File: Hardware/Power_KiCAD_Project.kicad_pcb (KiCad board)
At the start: 4 copper layers, 80 x 93.8 mm, 74 parts, among them IC1 STM32L562VET6Q, J1 XT60-M, J2 XT60-M, J3 XT60-M, J4 XT60-M, J5 XT60-M, J6 PJ-102AH, J7 XT60-M, J8 L717SDC37P1ACH4F, Q1 BSS84PH6327XTSA2, SW1 Reboot, U1 MCP9808_MSOP, U2 MCP9808_MSOP, U3 LM2678SX-5.0/NOPB, U4 LM2678SX-3.3/NOPB, U5 BQ76920PW, U6 PSMN2R6-40YS, U7 PSMN2R6-40YS, Y1 Crystal

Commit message: Added 3d step models to every component
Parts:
- removed IC1: STM32L562VET6Q, SamacSys_Parts:QFP50P1600X1600X160-100N
- removed U7: PSMN2R6-40YS, TO127P600X120-5N:TO127P600X120-5N
- removed VR1: T93YA103KT20, SamacSys_Parts:T93YA5K10
- added C30: 100nF, Capacitor_SMD:C_0603_1608Metric_Pad1.08x0.95mm_HandSolder, F.Cu at (328.5, 107.2)
- added C31: 100nF, Capacitor_SMD:C_0603_1608Metric_Pad1.08x0.95mm_HandSolder, F.Cu at (319.8, 115.0)
- added C32: 100nF, Capacitor_SMD:C_0603_1608Metric_Pad1.08x0.95mm_HandSolder, F.Cu at (319.8, 117.6)
- added C33: 100nF, Capacitor_SMD:C_0603_1608Metric_Pad1.08x0.95mm_HandSolder, F.Cu at (319.8, 107.5)
- added C34: 100nF, Capacitor_SMD:C_0603_1608Metric_Pad1.08x0.95mm_HandSolder, F.Cu at (328.5, 109.7)
- added C35: 100nF, Capacitor_SMD:C_0603_1608Metric_Pad1.08x0.95mm_HandSolder, F.Cu at (324.2, 115.0)
- added C36: 100nF, Capacitor_SMD:C_0603_1608Metric_Pad1.08x0.95mm_HandSolder, F.Cu at (182.9, 95.5)
- added Q2: BSS84PH6327XTSA2, Package_TO_SOT_SMD:SOT-23, F.Cu at (272.3, 130.0)
- added Q3: PSMN2R6-40YS, Package_TO_SOT_SMD:LFPAK33, F.Cu at (272.8, 125.3)
- added R18: 4.7k, Resistor_SMD:R_0603_1608Metric_Pad1.05x0.95mm_HandSolder, F.Cu at (324.2, 117.6)
- added R19: 4.7k, Resistor_SMD:R_0603_1608Metric_Pad1.05x0.95mm_HandSolder, F.Cu at (319.8, 120.1)
- added RV1: 10Ω to 2.2MΩ, RDT_Custom_Footprints:T93YA5K10, F.Cu at (256.4, 131.1)
- C1, C22: footprint Capacitor_SMD:C_0603_1608Metric -> Capacitor_SMD:C_0603_1608Metric_Pad1.08x0.95mm_HandSolder
- C10: value 35SVPF82M -> 16SVP330M; footprint SamacSys_Parts:16SVPT560M -> RDT_Custom_Footprints:16SVF1000M; moved to F.Cu
- C11, C12: value C0805C104M5RACTU -> 1μF; footprint SamacSys_Parts:CAPC2012X88N -> Capacitor_SMD:C_0603_1608Metric_Pad1.08x0.95mm_HandSolder; moved to F.Cu
- C13, C14: value CGA4C2C0G1H103J060AA -> 1μF; footprint SamacSys_Parts:CAPC2012X75N -> Capacitor_SMD:C_0603_1608Metric_Pad1.08x0.95mm_HandSolder; moved to F.Cu
- C15: value 16SVP330M -> 1μF; footprint SamacSys_Parts:16SVF1000M -> Capacitor_SMD:C_0603_1608Metric_Pad1.08x0.95mm_HandSolder; moved to F.Cu
- C16: value 6SVPC330M -> 1μF; footprint SamacSys_Parts:16SVF180M -> Capacitor_SMD:C_0603_1608Metric_Pad1.08x0.95mm_HandSolder; moved to F.Cu
- C17: value 1μF -> 4.7μF; footprint Capacitor_SMD:C_0603_1608Metric -> Capacitor_SMD:C_0603_1608Metric_Pad1.08x0.95mm_HandSolder
- C18, C20, C21: value 1μF -> 0.1μF; footprint Capacitor_SMD:C_0603_1608Metric -> Capacitor_SMD:C_0603_1608Metric_Pad1.08x0.95mm_HandSolder
- C19: value 1μF -> 10μF; footprint Capacitor_SMD:C_0603_1608Metric -> Capacitor_SMD:C_0603_1608Metric_Pad1.08x0.95mm_HandSolder
- C2: value 1uF -> 100nF; footprint Capacitor_SMD:C_0603_1608Metric -> Capacitor_SMD:C_0603_1608Metric_Pad1.08x0.95mm_HandSolder
- C23: value 0.1μF -> 1μF; footprint Capacitor_SMD:C_0603_1608Metric -> Capacitor_SMD:C_0603_1608Metric_Pad1.08x0.95mm_HandSolder
- C24: value 0.1μF -> 30pF; footprint Capacitor_SMD:C_0603_1608Metric -> Capacitor_SMD:C_0603_1608Metric_Pad1.08x0.95mm_HandSolder
- C25: value 4.7μF -> 30pF; footprint Capacitor_SMD:C_0603_1608Metric -> Capacitor_SMD:C_0603_1608Metric_Pad1.08x0.95mm_HandSolder
- C26: value 0.1μF -> 1uF; footprint Capacitor_SMD:C_0603_1608Metric -> Capacitor_SMD:C_0603_1608Metric_Pad1.08x0.95mm_HandSolder
- C27, C28: value 1μF -> 100nF; footprint Capacitor_SMD:C_0603_1608Metric -> Capacitor_SMD:C_0603_1608Metric_Pad1.08x0.95mm_HandSolder
- C29: value 10μF -> 100nF; footprint Capacitor_SMD:C_0603_1608Metric -> Capacitor_SMD:C_0603_1608Metric_Pad1.08x0.95mm_HandSolder
- C3, C4: value 100nF -> 35SVPF82M; footprint Capacitor_SMD:C_0603_1608Metric -> RDT_Custom_Footprints:16SVPT560M
- C5, C6: value 30pF -> C0805C104M5RACTU; footprint Capacitor_SMD:C_0603_1608Metric -> RDT_Custom_Footprints:CAPC2012X88N
- C7, C8: value 100nF -> CGA4C2C0G1H103J060AA; footprint Capacitor_SMD:C_0603_1608Metric -> RDT_Custom_Footprints:CAPC2012X75N
- C9: value 35SVPF82M -> 6SVPC330M; footprint SamacSys_Parts:16SVPT560M -> RDT_Custom_Footprints:16SVF180M; moved to F.Cu
- D1: value GREEN -> SBRD10200TR; footprint LED_SMD:LED_0603_1608Metric -> Package_TO_SOT_SMD:TO-252-2
- D2: value RED -> SBRD10200TR; footprint LED_SMD:LED_0603_1608Metric -> Package_TO_SOT_SMD:TO-252-2
- D3: value SBRD10200TR -> LED; footprint SBRD10200TR:DPAK228P1005X240-4N -> LED_SMD:LED_0603_1608Metric; moved to F.Cu
- D4: value SBRD10200TR -> 1N4148W-7-F; footprint SBRD10200TR:DPAK228P1005X240-4N -> Diode_SMD:D_SOD-123; moved to F.Cu
- D5: value LED -> GREEN
- D6: value 1N4148W-7-F -> RED; footprint SamacSys_Parts:SOD3716X145N -> LED_SMD:LED_0603_1608Metric
- J1: value XT60-M -> Barrel_Jack_MountingPin; footprint XT60-M:AMASS_XT60-M -> Connector_BarrelJack:BarrelJack_CUI_PJ-102AH_Horizontal; moved to F.Cu
- J2: value XT60-M -> XT60 Cell 5; footprint XT60-M:AMASS_XT60-M -> RDT_Custom_Footprints:AMASS_XT60-M; moved to F.Cu
- J3: value XT60-M -> XT60 Cell 4; footprint XT60-M:AMASS_XT60-M -> RDT_Custom_Footprints:AMASS_XT60-M; moved to F.Cu
- J4: value XT60-M -> XT60 Cell 3; footprint XT60-M:AMASS_XT60-M -> RDT_Custom_Footprints:AMASS_XT60-M; moved to F.Cu
- J5: value XT60-M -> XT60 Cell 2; footprint XT60-M:AMASS_XT60-M -> RDT_Custom_Footprints:AMASS_XT60-M; moved to F.Cu
- J6: value PJ-102AH -> XT60 Cell 1; footprint SamacSys_Parts:PJ-102AH -> RDT_Custom_Footprints:AMASS_XT60-M; moved to F.Cu
- J7: value XT60-M -> XT60 To External Switch; footprint XT60-M:AMASS_XT60-M -> RDT_Custom_Footprints:AMASS_XT60-M
- J8: footprint SamacSys_Parts:L717SDC37P1ACH4F -> RDT_Custom_Footprints:L717SDC37P1ACH4F; moved to F.Cu
- L1: value SRP1270-8R2M -> MSS1210-153MEB; footprint SamacSys_Parts:INDPM137129X700N -> RDT_Custom_Footprints:IND_MSS1210-153MEB; moved to F.Cu
- L2: value MSS1210-153MEB -> SRP1270-8R2M; footprint MSS1210-153MEB:IND_MSS1210-153MEB -> RDT_Custom_Footprints:INDPM137129X700N; moved to F.Cu
- Q1: value BSS84PH6327XTSA2 -> PSMN2R6-40YS; footprint SamacSys_Parts:SOT95P240X110-3N -> Package_TO_SOT_SMD:LFPAK33
- R1, R11, R2: value 1k5Ω -> 100Ω; footprint Resistor_SMD:R_0603_1608Metric -> Resistor_SMD:R_0603_1608Metric_Pad1.05x0.95mm_HandSolder
- R10: value WSHP28185L000FEA -> 5mΩ 10W
- R12: value 10kΩ -> 1MΩ; footprint Resistor_SMD:R_0603_1608Metric -> Resistor_SMD:R_0603_1608Metric_Pad1.05x0.95mm_HandSolder
- R13, R15: value 100Ω -> 1MΩ; footprint Resistor_SMD:R_0603_1608Metric -> Resistor_SMD:R_0603_1608Metric_Pad1.05x0.95mm_HandSolder
- R14: value 1MΩ -> 10kΩ; footprint Resistor_SMD:R_0603_1608Metric -> Resistor_SMD:R_0603_1608Metric_Pad1.05x0.95mm_HandSolder
- R16, R17: value 1MΩ -> 1k5Ω; footprint Resistor_SMD:R_0603_1608Metric -> Resistor_SMD:R_0603_1608Metric_Pad1.05x0.95mm_HandSolder
- R3, R4, R5, R6, R8, R9: footprint Resistor_SMD:R_0603_1608Metric -> Resistor_SMD:R_0603_1608Metric_Pad1.05x0.95mm_HandSolder
- R7: value 100Ω -> 1k5Ω; footprint Resistor_SMD:R_0603_1608Metric -> Resistor_SMD:R_0603_1608Metric_Pad1.05x0.95mm_HandSolder
- SW1: footprint Button_Switch_SMD:SW_Push_1P1T_NO_6x6mm_H9.5mm -> Button_Switch_SMD:SW_SPST_PTS645
- U3, U4: moved to F.Cu
- U6: value PSMN2R6-40YS -> STM32L562VET; footprint TO127P600X120-5N:TO127P600X120-5N -> Package_QFP:LQFP-100_14x14mm_P0.5mm
- Y1: value Crystal -> 32MHz; footprint Crystal:Crystal_HC49-4H_Vertical -> Crystal:Crystal_SMD_2012-2Pin_2.0x1.2mm_HandSoldering
- moved R17 210.7 mm to (328.5, 112.2), turned to 0 degrees
- moved D6 207.5 mm to (324.0, 120.1), turned to 0 degrees
- moved C29 205.2 mm to (324.2, 110.0), turned to 0 degrees
- moved D5 205.2 mm to (328.4, 114.7), turned to 0 degrees
- moved C27 203.7 mm to (328.6, 104.7), turned to 0 degrees
- moved R16 202.9 mm to (324.2, 112.5), turned to 0 degrees
- moved C24 200.0 mm to (324.3, 104.7), turned to 0 degrees
- moved C28 199.1 mm to (319.8, 112.5), turned to 0 degrees
- moved C26 196.4 mm to (324.2, 107.5)
- moved C25 193.9 mm to (319.8, 110.0), turned to 0 degrees
- moved Y1 187.1 mm to (319.9, 104.8), turned to 0 degrees
- moved U6 180.2 mm to (308.4, 112.7), turned to 0 degrees
- moved R15 173.6 mm to (284.4, 132.2), turned to 0 degrees
- moved R11 168.3 mm to (292.1, 118.8)
- moved C23 165.6 mm to (287.7, 122.2), turned to 0 degrees
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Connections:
- C1 pad 2: /Pack- -> GND
- C10 pad 1: /PACK_M5 -> +5V
- C10 pad 2: /Pack- -> GND
- C11 pad 1: /PACK_M5 -> /LiPo Pack Monitor/VC5
- C11 pad 2: /Pack- -> /LiPo Pack Monitor/VC4
- C12 pad 1: /PACK_M5 -> /LiPo Pack Monitor/VC4
- C12 pad 2: /Pack- -> /LiPo Pack Monitor/VC3
- C13 pad 1: Net-(C13-Pad1) -> /LiPo Pack Monitor/VC3
- C13 pad 2: Net-(C13-Pad2) -> /LiPo Pack Monitor/VC2
- C14 pad 1: Net-(C14-Pad1) -> /LiPo Pack Monitor/VC2
- C14 pad 2: Net-(C14-Pad2) -> /LiPo Pack Monitor/VC1
- C15 pad 1: +5V -> /LiPo Pack Monitor/VC1
- C15 pad 2: /Pack- -> GNDREF
- C16 pad 1: +3V3 -> GNDREF
- C16 pad 2: /Pack- -> /LiPo Pack Monitor/VC0
- C17 pad 1: /LiPo Pack Monitor/VC5 -> GNDREF
- C17 pad 2: /LiPo Pack Monitor/VC4 -> Net-(C17-Pad2)
- C18 pad 1: /LiPo Pack Monitor/VC4 -> Net-(C18-Pad1)
- C18 pad 2: /LiPo Pack Monitor/VC3 -> GNDREF
- C19 pad 1: /LiPo Pack Monitor/VC3 -> GNDREF
- C19 pad 2: /LiPo Pack Monitor/VC2 -> Net-(C19-Pad2)
- C2 pad 1: /Pack- -> +3V3
- C2 pad 2: +3V3 -> GND
- C20 pad 1: /LiPo Pack Monitor/VC2 -> Net-(C20-Pad1)
- C20 pad 2: /LiPo Pack Monitor/VC1 -> Net-(C18-Pad1)
- C21 pad 1: /LiPo Pack Monitor/VC1 -> GNDREF
- C21 pad 2: GND -> Net-(C20-Pad1)
- C22 pad 1: GND -> GNDREF
- C22 pad 2: /LiPo Pack Monitor/VC0 -> /PACK_M5
- C23 pad 1: /LiPo Pack Monitor/SRP -> GNDREF
- C23 pad 2: GND -> Net-(C23-Pad2)
- C24 pad 1: /LiPo Pack Monitor/SRN -> Net-(C24-Pad1)
- C24 pad 2: /LiPo Pack Monitor/SRP -> GND
- C25 pad 1: GND -> Net-(C25-Pad1)
- C25 pad 2: Net-(C25-Pad2) -> GND
- C26 pad 1: GND -> +3V3
- C26 pad 2: /LiPo Pack Monitor/SRN -> GND
- C27 pad 1: GND -> +3V3
- C27 pad 2: Net-(C27-Pad2) -> GND
- C28 pad 1: GND -> +3V3
- C28 pad 2: /PACK_M5 -> GND
- C29 pad 1: GND -> +3V3
- C29 pad 2: /LiPo Pack Monitor/BAT -> GND
- C3 pad 1: /Pack- -> /PACK_M5
- C3 pad 2: +3V3 -> GND
- C4 pad 1: /Pack- -> /PACK_M5
- C4 pad 2: +3V3 -> GND
- C5 pad 1: /Pack- -> /PACK_M5
- C5 pad 2: Net-(C5-Pad2) -> GND
- C6 pad 1: /Pack- -> /PACK_M5
- C6 pad 2: Net-(C6-Pad2) -> GND
- C7 pad 1: +3V3 -> Net-(C7-Pad1)
- C7 pad 2: /Pack- -> Net-(C7-Pad2)
- C8 pad 1: /NRST -> Net-(C8-Pad1)
- C8 pad 2: /Pack- -> Net-(C8-Pad2)
- C9 pad 1: /PACK_M5 -> +3V3
- C9 pad 2: /Pack- -> GND
- D1 pad 1: Net-(D1-Pad1) -> GND
- D1 pad 2: Net-(D1-Pad2) -> Net-(C7-Pad2)
- D2 pad 1: Net-(D2-Pad1) -> GND
- D2 pad 2: Net-(D2-Pad2) -> Net-(C8-Pad2)
- D3 pad 1: /Pack- -> Net-(D3-Pad1)
- D3 pad 2: Net-(C13-Pad2) -> Net-(C17-Pad2)
- D4 pad 1: /Pack- -> Net-(D4-Pad1)
- D4 pad 2: Net-(C14-Pad2) -> Net-(D4-Pad2)
- D5 pad 2: Net-(C25-Pad2) -> Net-(D5-Pad2)
- J1 pad 1: /PACK_M4 -> /PACK_M5
- J1 pad 2: /PACK_M5 -> GNDREF
- J2 pad 1: /PACK_M3 -> /PACK_M4
- J2 pad 2: /PACK_M4 -> /PACK_M5
- J3 pad 1: /PACK_M2 -> /PACK_M3
- J3 pad 2: /PACK_M3 -> /PACK_M4
- J4 pad 1: /PACK_M1 -> /PACK_M2
- J4 pad 2: /PACK_M2 -> /PACK_M3
- J5 pad 1: GND -> /PACK_M1
- J5 pad 2: /PACK_M1 -> /PACK_M2
- J6 pad 1: /PACK_M5 -> GNDREF
- J6 pad 2: /Pack- -> /PACK_M1
- J7 pad 1: GND -> GNDREF
- J7 pad 2: GND -> Net-(J7-Pad2)
- J8 pad 1: /Pack- -> GND
- J8 pad 10: (no net) -> Net-(J8-Pad10)
- J8 pad 11: (no net) -> Net-(J8-Pad11)
- J8 pad 12: (no net) -> Net-(J8-Pad12)
- J8 pad 13: (no net) -> Net-(J8-Pad13)
- J8 pad 14: (no net) -> Net-(J8-Pad14)
- J8 pad 15: (no net) -> Net-(J8-Pad15)
- J8 pad 16: (no net) -> Net-(J8-Pad16)
- J8 pad 17: (no net) -> Net-(J8-Pad17)
- J8 pad 19: /Pack- -> GND
- J8 pad 21: (no net) -> /DSUB-37_Bus/t_mosi
- J8 pad 22: (no net) -> /DSUB-37_Bus/t_clk
- J8 pad 23: /SWCLK -> /STM32L562VET6Q 1/DEBUG_SWCLK
- J8 pad 24: /Alert_sda -> /DSUB-37_Bus/Alert_sda
- J8 pad 25: /NRST -> /DSUB-37_Bus/NRST
- J8 pad 26: (no net) -> /DSUB-37_Bus/Fire_redundant
- J8 pad 27: (no net) -> Net-(J8-Pad27)
- J8 pad 28: (no net) -> Net-(J8-Pad28)
- J8 pad 29: (no net) -> Net-(J8-Pad29)
- J8 pad 3: (no net) -> /DSUB-37_Bus/t_miso
- J8 pad 30: (no net) -> Net-(J8-Pad30)
- J8 pad 31: (no net) -> Net-(J8-Pad31)
- J8 pad 32: (no net) -> Net-(J8-Pad32)
- J8 pad 33: (no net) -> Net-(J8-Pad33)
- J8 pad 34: (no net) -> Net-(J8-Pad34)
- J8 pad 35: (no net) -> Net-(J8-Pad35)
- J8 pad 36: (no net) -> Net-(J8-Pad36)
- J8 pad 4: /SWDIO -> /STM32L562VET6Q 1/DEBUG_SWDIO
- J8 pad 5: /Alert_scl -> /DSUB-37_Bus/Alert_scl
- J8 pad 6: /Alert_active -> /DSUB-37_Bus/Alert_Active
- J8 pad 7: (no net) -> /DSUB-37_Bus/Fire
- J8 pad 8: (no net) -> Net-(J8-Pad8)
- J8 pad 9: (no net) -> Net-(J8-Pad9)
- J8 pad MH1: /Pack- -> GND
- J8 pad MH2: /Pack- -> GND
- L1 pad 1: Net-(C14-Pad2) -> Net-(C7-Pad2)
- L1 pad 2: +3V3 -> +5V
- L2 pad 1: Net-(C13-Pad2) -> Net-(C8-Pad2)
- L2 pad 2: +5V -> +3V3
- Q1 pad 1: GND -> Net-(Q1-Pad1)
- Q1 pad 2: Net-(D6-Pad2) -> Net-(Q1-Pad1)
- Q1 pad 3: Net-(Q1-Pad3) -> Net-(Q1-Pad1)
- R1 pad 1: Net-(D1-Pad1) -> /PACK_M5
- R1 pad 2: /Pack- -> /LiPo Pack Monitor/VC5
- R10 pad 1: GND -> Net-(J7-Pad2)
- R10 pad 2: Net-(R10-Pad2) -> Net-(Q1-Pad1)
- R11 pad 1: Net-(D5-Pad1) -> Net-(C20-Pad1)
- R11 pad 2: GND -> Net-(Q1-Pad1)
- R12 pad 1: /LiPo Pack Monitor/TS1 -> Net-(Q1-Pad4)
- R12 pad 2: Net-(R12-Pad2) -> Net-(Q1-Pad1)
- R13 pad 1: /LiPo Pack Monitor/SRN -> Net-(D4-Pad1)
- R13 pad 2: Net-(R10-Pad2) -> Net-(D4-Pad2)
- R14 pad 2: Net-(R10-Pad2) -> Net-(R14-Pad2)
- R15 pad 1: /PACK_M5 -> Net-(D4-Pad1)
- R15 pad 2: /LiPo Pack Monitor/BAT -> GNDREF
- R16 pad 1: Net-(D6-Pad1) -> Net-(D5-Pad1)
- R16 pad 2: Net-(D6-Pad2) -> GND
- R17 pad 2: /Pack- -> GND
- R2 pad 1: Net-(D2-Pad1) -> /PACK_M4
- R2 pad 2: /Pack- -> /LiPo Pack Monitor/VC4
- R3 pad 1: /PACK_M5 -> /PACK_M3
- R3 pad 2: /LiPo Pack Monitor/VC5 -> /LiPo Pack Monitor/VC3
- R4 pad 1: /PACK_M4 -> /PACK_M2
- R4 pad 2: /LiPo Pack Monitor/VC4 -> /LiPo Pack Monitor/VC2
- R5 pad 1: /PACK_M3 -> /PACK_M1
- R5 pad 2: /LiPo Pack Monitor/VC3 -> /LiPo Pack Monitor/VC1
- R6 pad 1: /PACK_M2 -> GNDREF
- R6 pad 2: /LiPo Pack Monitor/VC2 -> /LiPo Pack Monitor/VC0
- R7 pad 1: /PACK_M1 -> Net-(D3-Pad1)
- R7 pad 2: /LiPo Pack Monitor/VC1 -> GNDREF
- R8 pad 1: GND -> Net-(C18-Pad1)
- R8 pad 2: /LiPo Pack Monitor/VC0 -> Net-(J7-Pad2)
- R9 pad 1: /LiPo Pack Monitor/SRP -> /PACK_M5
- R9 pad 2: GND -> Net-(C19-Pad2)
- SW1 pad 1: Net-(R12-Pad2) -> Net-(R14-Pad2)
- U1 pad 4: /Pack- -> GND
- U1 pad 5: /Pack- -> GND
- U1 pad 6: /Pack- -> GND
- U1 pad 7: /Pack- -> GND
- U2 pad 4: /Pack- -> GND
- U2 pad 5: /Pack- -> GND
- U2 pad 6: /Pack- -> GND
- U3 pad 1: Net-(C13-Pad2) -> Net-(C7-Pad2)
- U3 pad 3: Net-(C13-Pad1) -> Net-(C7-Pad1)
- U3 pad 4: /Pack- -> GND
- U3 pad 7: (no net) -> Net-(U3-Pad7)
- U4 pad 1: Net-(C14-Pad2) -> Net-(C8-Pad2)
- U4 pad 3: Net-(C14-Pad1) -> Net-(C8-Pad1)
- U4 pad 4: /Pack- -> GND
- U4 pad 7: (no net) -> Net-(U4-Pad7)
- U5 pad 1: Net-(R14-Pad1) -> Net-(Q1-Pad4)
- U5 pad 10: /LiPo Pack Monitor/BAT -> Net-(C19-Pad2)
- U5 pad 11: (no net) -> Net-(U5-Pad11)
- U5 pad 18: /LiPo Pack Monitor/SRP -> Net-(C18-Pad1)
- U5 pad 19: /LiPo Pack Monitor/SRN -> Net-(C20-Pad1)
- U5 pad 2: Net-(Q1-Pad3) -> Net-(Q2-Pad3)
- U5 pad 20: (no net) -> /BATT_ALERT
- U5 pad 3: GND -> GNDREF
- U5 pad 4: (no net) -> /LiPo Pack Monitor/I2C_SDA
- U5 pad 5: (no net) -> /LiPo Pack Monitor/I2C_SCL
- U5 pad 6: /LiPo Pack Monitor/TS1 -> Net-(R14-Pad1)
- U5 pad 7: Net-(C27-Pad2) -> Net-(C23-Pad2)
- U5 pad 8: Net-(C25-Pad2) -> Net-(C17-Pad2)
- U6 pad 1: Net-(R10-Pad2) -> Net-(U6-Pad1)
- U6 pad 2: Net-(R10-Pad2) -> Net-(U6-Pad2)
- U6 pad 3: Net-(R10-Pad2) -> Net-(U6-Pad3)
- U6 pad 4: Net-(R14-Pad1) -> Net-(U6-Pad4)
- Y1 pad 1: Net-(C5-Pad2) -> Net-(C24-Pad1)
- Y1 pad 2: Net-(C6-Pad2) -> Net-(C25-Pad1)
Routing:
- net /Pack-: track 301.0 -> 0.00 mm
- net +3V3: track 281.2 -> 0.00 mm, vias 1 -> 0
- net /PACK_M5: track 209.9 -> 0.00 mm
- net +5V: track 135.7 -> 0.00 mm
- net GND: track 125.7 -> 0.00 mm, vias 2 -> 0
- net /I2C_SDA: track 74.6 -> 0.00 mm, vias 2 -> 0
- net /I2C_SCL: track 73.3 -> 0.00 mm, vias 2 -> 0
- net /TEMP_ALERT_1: track 69.9 -> 0.00 mm, vias 2 -> 0
- net /LiPo Pack Monitor/VC1: track 67.7 -> 0.00 mm, vias 2 -> 0
- net Net-(C13-Pad2): track 67.0 -> 0.00 mm
- net /SWCLK: track 62.3 -> 0.00 mm, vias 1 -> 0
- net Net-(C14-Pad2): track 58.7 -> 0.00 mm
- net /SWDIO: track 57.8 -> 0.00 mm, vias 1 -> 0
- net /LiPo Pack Monitor/VC3: track 57.2 -> 0.00 mm, vias 2 -> 0
- net /TEMP_ALERT_2: track 56.3 -> 0.00 mm, vias 2 -> 0
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- added copper zone on 3.3V.Cu, net +3V3
- added copper zone on GND.Cu, net GND
- removed copper zone on ground, net /Pack-
- removed copper zone on ground, net GND
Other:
- board size 80 x 93.8 mm -> 80 x 93.2 mm
- net class DIFF_90_USB added: clearance 0.05, trace_width 0.175006, via_dia 0.4, via_drill 0.2
- net class Default: clearance 0.2 -> 0.05
- rule pad_to_mask_clearance: 0 -> 0.051
- rule trace_clearance: 0.2 -> 0.05
- rule trace_min: 0.2 -> 0.09
- rule via_min_drill: 0.3 -> 0.2

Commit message: Progress made to the battery section
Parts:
- moved R11 184.2 mm to (108.0, 113.0)
- moved R8 181.6 mm to (108.0, 114.8)
- moved C21 179.3 mm to (104.2, 113.0)
- moved R12 173.0 mm to (118.5, 87.8), turned to 180 degrees
- moved C20 172.5 mm to (104.2, 114.8)
- moved Q1 168.4 mm to (114.2, 87.0), turned to 180 degrees
- moved C18 168.2 mm to (104.2, 116.5)
- moved Q3 167.4 mm to (109.8, 87.0)
- moved C23 166.6 mm to (124.0, 91.1), turned to 90 degrees
- moved C19 160.6 mm to (135.4, 88.0), turned to 180 degrees
- moved Q2 160.5 mm to (118.5, 84.2)
- moved C17 159.6 mm to (131.9, 85.2), turned to 180 degrees
- moved R7 158.1 mm to (134.9, 83.2)
- moved R10 154.8 mm to (110.8, 118.5)
- moved R14 151.9 mm to (142.0, 100.2)
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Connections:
- U6 pad 91: /STM32L562VET6Q 1/I2C1_EN -> /DSUB-37_Bus/Alert_Active
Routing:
- net /PACK_M5: track 0.00 -> 54.2 mm
- net /LiPo Pack Monitor/VC0: track 0.00 -> 28.8 mm
- net /LiPo Pack Monitor/VC1: track 0.00 -> 27.8 mm
- net /LiPo Pack Monitor/VC5: track 0.00 -> 26.9 mm
- net /PACK_M4: track 0.00 -> 22.3 mm
- net /PACK_M2: track 0.00 -> 22.2 mm
- net /LiPo Pack Monitor/VC4: track 0.00 -> 21.0 mm
- net /LiPo Pack Monitor/VC2: track 0.00 -> 20.1 mm
- net /PACK_M3: track 0.00 -> 15.1 mm
- net /PACK_M1: track 0.00 -> 15.1 mm
- net GNDREF: track 0.00 -> 12.4 mm, vias 0 -> 8
- net /LiPo Pack Monitor/VC3: track 0.00 -> 12.4 mm
- net Net-(C19-Pad2): track 0.00 -> 9.22 mm
- net Net-(C17-Pad2): track 0.00 -> 8.57 mm
- net Net-(D3-Pad1): track 0.00 -> 1.71 mm
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- added copper zone on GND.Cu, net GNDREF

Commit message: Routed battery side of pcb
GNDREF has its own island on the inner copper layer, separate from the rest of the components which will get a normal GND inner copper layer
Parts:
- moved U1 235.0 mm to (90.2, 136.0), turned to 180 degrees
- moved R15 172.5 mm to (119.2, 82.2), turned to 270 degrees
- moved R13 171.8 mm to (119.4, 85.6), turned to 45 degrees
- moved D4 164.4 mm to (123.2, 82.5)
- moved U2 127.5 mm to (134.2, 91.7)
- moved C2 127.5 mm to (140.0, 90.7)
- moved C26 106.3 mm to (218.4, 96.5)
- moved C29 106.3 mm to (218.4, 99.0)
- moved C25 106.3 mm to (214.1, 99.0)
- moved C27 106.3 mm to (222.9, 93.7)
- moved C33 106.3 mm to (214.1, 96.5)
- moved Y1 106.3 mm to (214.1, 93.8)
- moved C24 106.3 mm to (218.5, 93.7)
- moved C30 106.3 mm to (222.8, 96.2)
- moved C34 106.3 mm to (222.8, 98.7)
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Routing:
- net Net-(Q1-Pad4): track 0.00 -> 35.4 mm
- net Net-(D4-Pad1): track 0.00 -> 32.8 mm
- net GNDREF: track 12.4 -> 39.0 mm, vias 8 -> 14
- net Net-(Q1-Pad1): track 1.30 -> 25.3 mm
- net /LiPo Pack Monitor/VC1: track 27.8 -> 48.0 mm, vias 0 -> 2
- net Net-(R14-Pad1): track 0.00 -> 16.5 mm, vias 0 -> 2
- net /LiPo Pack Monitor/VC5: track 26.9 -> 14.1 mm
- net /PACK_M5: track 54.2 -> 42.2 mm
- net Net-(R14-Pad2): track 0.00 -> 10.3 mm
- net /LiPo Pack Monitor/VC0: track 28.8 -> 38.1 mm
- net Net-(D4-Pad2): track 0.00 -> 8.11 mm
- net /LiPo Pack Monitor/VC4: track 21.0 -> 13.2 mm
- net Net-(C19-Pad2): track 9.22 -> 1.91 mm
- net Net-(Q1-Pad5): track 0.00 -> 7.19 mm
- net Net-(C17-Pad2): track 8.57 -> 1.53 mm
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- added copper zone on GND.Cu, net Net-(J7-Pad2)
- removed copper zone on GND.Cu, net GND

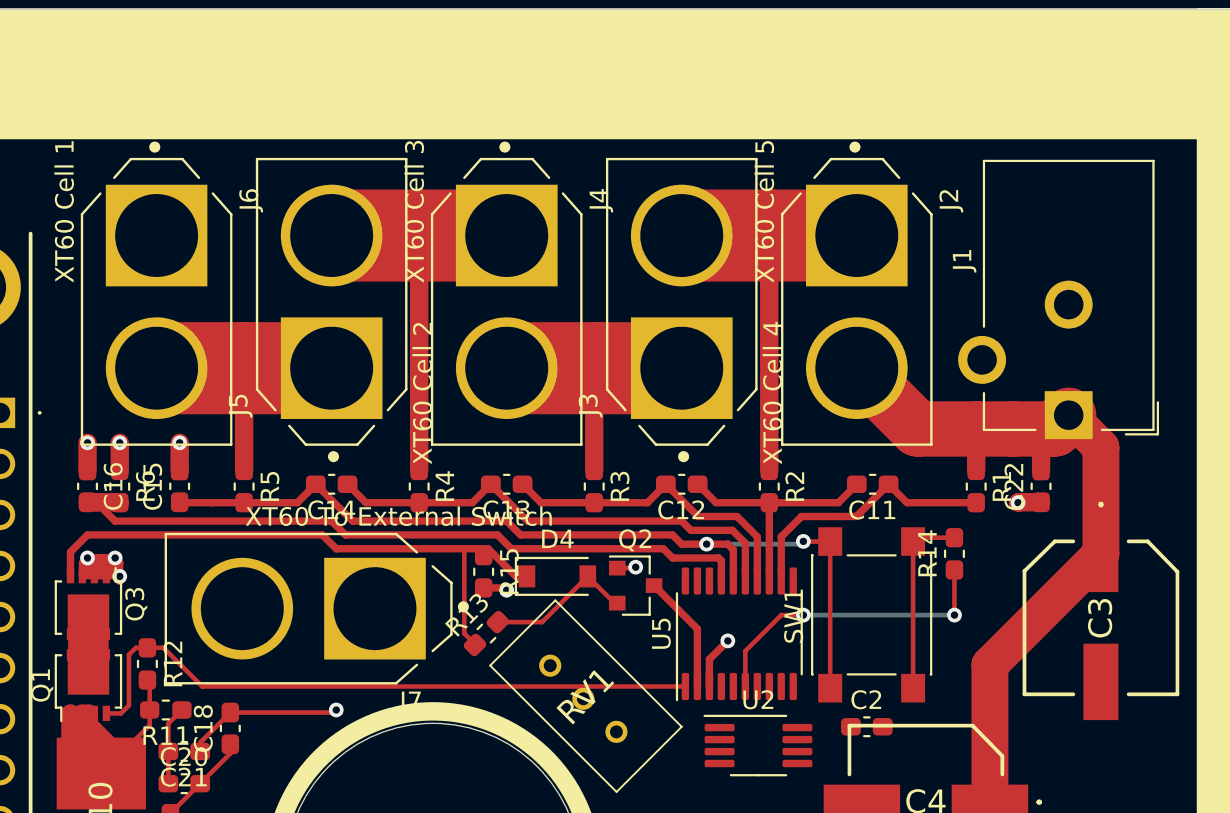
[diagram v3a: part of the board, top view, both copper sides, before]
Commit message: Increased spacing between XT60 connectors
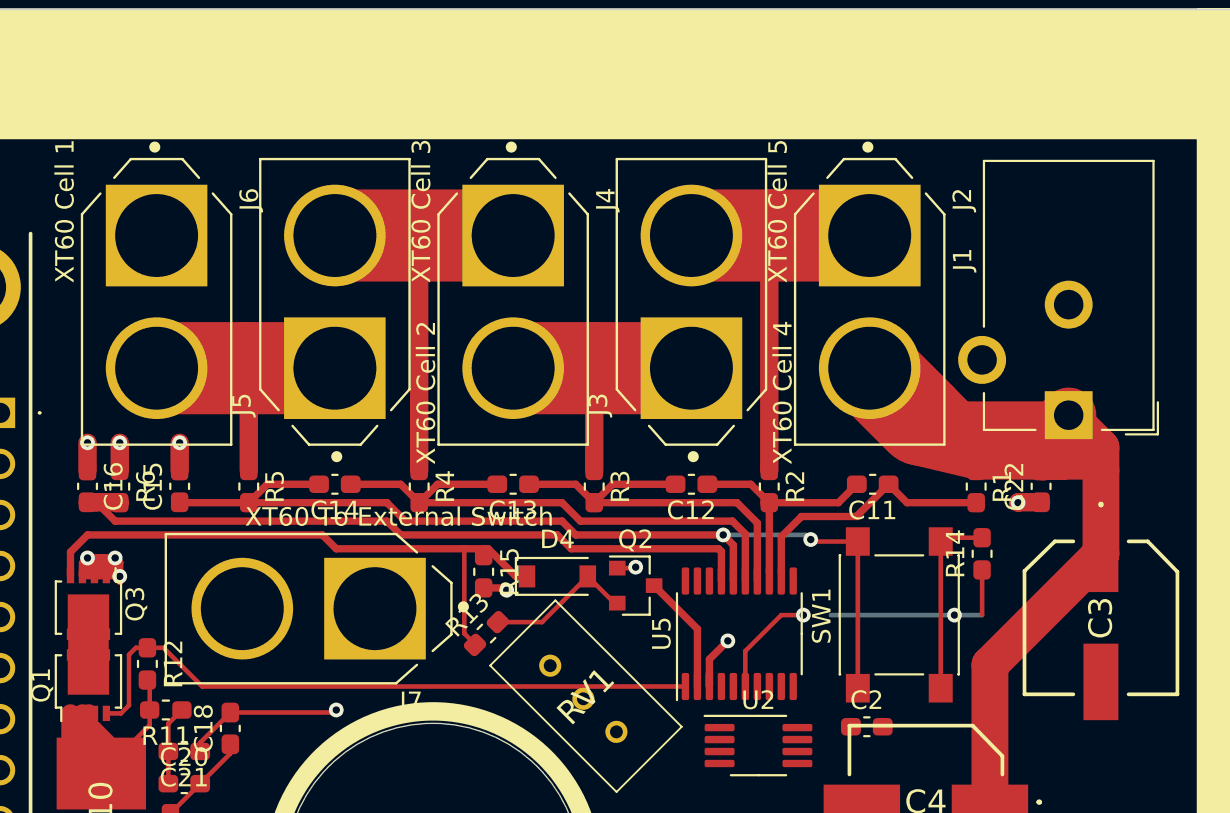
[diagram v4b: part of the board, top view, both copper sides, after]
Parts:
- moved R14 1.50 mm to (146.3, 81.3)
- moved SW1 1.50 mm to (141.8, 84.6)
- moved J2 0.70 mm to (140.2, 67.6)
- moved C12 0.53 mm to (130.5, 77.5)
- moved J3 0.53 mm to (130.5, 67.6)
- moved C13 0.35 mm to (120.8, 77.5)
- moved J4 0.35 mm to (120.8, 67.6)
- moved R5 0.25 mm to (106.5, 77.6)
- moved C14 0.17 mm to (111.2, 77.5)
- moved J5 0.17 mm to (111.2, 67.6)
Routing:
- net /PACK_M5: track 42.2 -> 65.4 mm
- net /LiPo Pack Monitor/VC1: track 48.0 -> 52.6 mm
- net /LiPo Pack Monitor/VC3: track 16.6 -> 21.2 mm
- net /LiPo Pack Monitor/VC2: track 25.3 -> 29.7 mm
- net /LiPo Pack Monitor/VC4: track 13.2 -> 12.7 mm

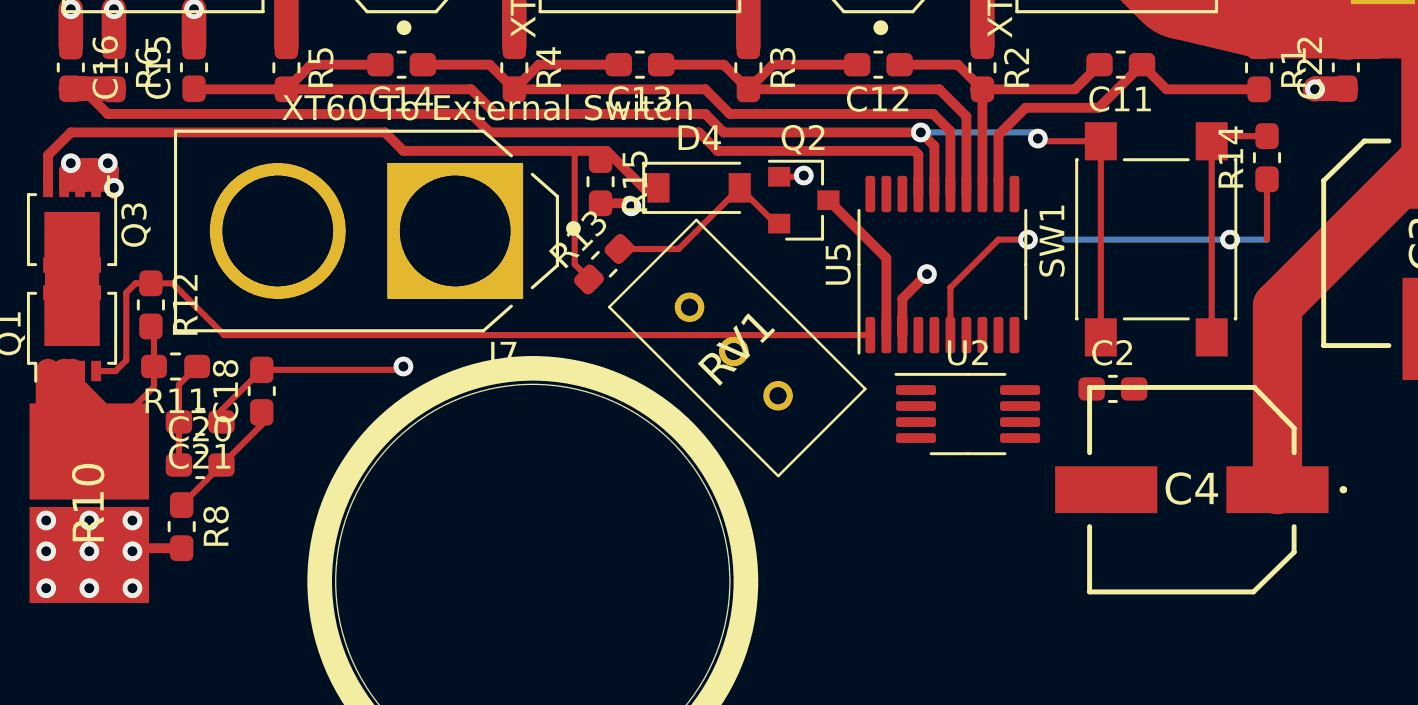
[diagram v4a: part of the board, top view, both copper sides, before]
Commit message: Adjusted GNDREF and GND copper zones
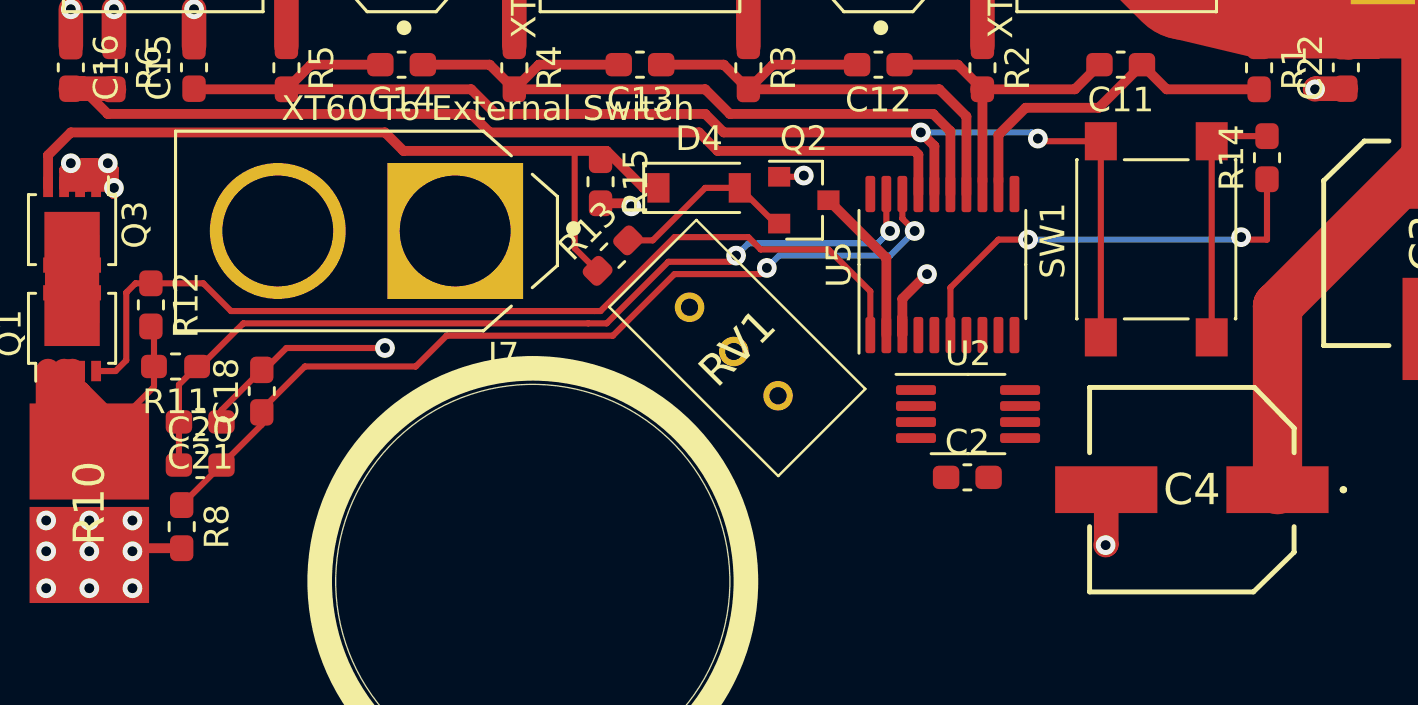
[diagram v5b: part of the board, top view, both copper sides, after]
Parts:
- moved C2 6.91 mm to (134.1, 94.2)
- moved R13 0.49 mm to (119.8, 85.2)
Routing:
- net Net-(C20-Pad1): track 4.31 -> 36.3 mm, vias 0 -> 2
- net Net-(C18-Pad1): track 5.25 -> 36.8 mm, vias 0 -> 2
- net Net-(Q1-Pad4): track 35.4 -> 38.9 mm
- net GND: track 0.00 -> 2.26 mm, vias 0 -> 1
- net Net-(R14-Pad1): track 16.5 -> 18.1 mm
- added copper zone on GND.Cu, net GND
